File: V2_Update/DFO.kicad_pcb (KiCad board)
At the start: 2 copper layers, 19.8 x 19.6 mm, 18 parts, among them U1 Si5351A-B-GT, U2 ATmega328-A, X1 ASE-25MHz

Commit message: update
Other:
- board text added: "JP1"
- board text added: "JP2"
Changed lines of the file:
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@@
     (fp_line (start -0.261252 -0.735) (end 0.261252 -0.735) (layer "F.SilkS") (width 0.12))
     (fp_line (start -0.261252 0.735) (end 0.261252 0.735) (layer "F.SilkS") (width 0.12))
+    (fp_line (start -1.7 -0.98) (end 1.7 -0.98) (layer "F.CrtYd") (width 0.05))
+    (fp_line (start 1.7 0.98) (end -1.7 0.98) (layer "F.CrtYd") (width 0.05))
     (fp_line (start -1.7 0.98) (end -1.7 -0.98) (layer "F.CrtYd") (width 0.05))
     (fp_line (start 1.7 -0.98) (end 1.7 0.98) (layer "F.CrtYd") (width 0.05))
-    (fp_line (start 1.7 0.98) (end -1.7 0.98) (layer "F.CrtYd") (width 0.05))
-    (fp_line (start -1.7 -0.98) (end 1.7 -0.98) (layer "F.CrtYd") (width 0.05))
+    (fp_line (start 1 -0.625) (end 1 0.625) (layer "F.Fab") (width 0.1))
+    (fp_line (start -1 0.625) (end -1 -0.625) (layer "F.Fab") (width 0.1))
+    (fp_line (start 1 0.625) (end -1 0.625) (layer "F.Fab") (width 0.1))
     (fp_line (start -1 -0.625) (end 1 -0.625) (layer "F.Fab") (width 0.1))
-    (fp_line (start -1 0.625) (end -1 -0.625) (layer "F.Fab") (width 0.1))
-    (fp_line (start 1 -0.625) (end 1 0.625) (layer "F.Fab") (width 0.1))
-    (fp_line (start 1 0.625) (end -1 0.625) (layer "F.Fab") (width 0.1))
     (pad "1" smd roundrect (at -0.95 0 90) (size 1 1.45) (layers "F.Cu" "F.Paste" "F.Mask") (roundrect_rratio 0.25)
       (net 35 "CLK_OUT_SI5351"))
@@
     (fp_line (start -0.261252 -0.735) (end 0.261252 -0.735) (layer "F.SilkS") (width 0.12))
     (fp_line (start -0.261252 0.735) (end 0.261252 0.735) (layer "F.SilkS") (width 0.12))
+    (fp_line (start 1.7 -0.98) (end 1.7 0.98) (layer "F.CrtYd") (width 0.05))
+    (fp_line (start -1.7 -0.98) (end 1.7 -0.98) (layer "F.CrtYd") (width 0.05))
+    (fp_line (start 1.7 0.98) (end -1.7 0.98) (layer "F.CrtYd") (width 0.05))
     (fp_line (start -1.7 0.98) (end -1.7 -0.98) (layer "F.CrtYd") (width 0.05))
-    (fp_line (start 1.7 -0.98) (end 1.7 0.98) (layer "F.CrtYd") (width 0.05))
-    (fp_line (start 1.7 0.98) (end -1.7 0.98) (layer "F.CrtYd") (width 0.05))
-    (fp_line (start -1.7 -0.98) (end 1.7 -0.98) (layer "F.CrtYd") (width 0.05))
+    (fp_line (start -1 0.625) (end -1 -0.625) (layer "F.Fab") (width 0.1))
     (fp_line (start -1 -0.625) (end 1 -0.625) (layer "F.Fab") (width 0.1))
-    (fp_line (start -1 0.625) (end -1 -0.625) (layer "F.Fab") (width 0.1))
     (fp_line (start 1 -0.625) (end 1 0.625) (layer "F.Fab") (width 0.1))
     (fp_line (start 1 0.625) (end -1 0.625) (layer "F.Fab") (width 0.1))
@@
     (fp_line (start -0.261252 -0.735) (end 0.261252 -0.735) (layer "F.SilkS") (width 0.12))
     (fp_line (start -0.261252 0.735) (end 0.261252 0.735) (layer "F.SilkS") (width 0.12))
+    (fp_line (start -1.7 0.98) (end -1.7 -0.98) (layer "F.CrtYd") (width 0.05))
     (fp_line (start 1.7 -0.98) (end 1.7 0.98) (layer "F.CrtYd") (width 0.05))
-    (fp_line (start -1.7 0.98) (end -1.7 -0.98) (layer "F.CrtYd") (width 0.05))
     (fp_line (start 1.7 0.98) (end -1.7 0.98) (layer "F.CrtYd") (width 0.05))
     (fp_line (start -1.7 -0.98) (end 1.7 -0.98) (layer "F.CrtYd") (width 0.05))
+    (fp_line (start 1 -0.625) (end 1 0.625) (layer "F.Fab") (width 0.1))
+    (fp_line (start 1 0.625) (end -1 0.625) (layer "F.Fab") (width 0.1))
     (fp_line (start -1 0.625) (end -1 -0.625) (layer "F.Fab") (width 0.1))
     (fp_line (start -1 -0.625) (end 1 -0.625) (layer "F.Fab") (width 0.1))
-    (fp_line (start 1 0.625) (end -1 0.625) (layer "F.Fab") (width 0.1))
-    (fp_line (start 1 -0.625) (end 1 0.625) (layer "F.Fab") (width 0.1))
     (pad "1" smd roundrect (at -0.95 0) (size 1 1.45) (layers "F.Cu" "F.Paste" "F.Mask") (roundrect_rratio 0.25))
     (pad "2" smd roundrect (at 0.95 0) (size 1 1.45) (layers "F.Cu" "F.Paste" "F.Mask") (roundrect_rratio 0.25)
@@
       (effects (font (size 0.5 0.5) (thickness 0.08)))
     )
+    (fp_line (start -0.261252 0.735) (end 0.261252 0.735) (layer "F.SilkS") (width 0.12))
     (fp_line (start -0.261252 -0.735) (end 0.261252 -0.735) (layer "F.SilkS") (width 0.12))
-    (fp_line (start -0.261252 0.735) (end 0.261252 0.735) (layer "F.SilkS") (width 0.12))
-    (fp_line (start -1.7 0.98) (end -1.7 -0.98) (layer "F.CrtYd") (width 0.05))
+    (fp_line (start -1.7 -0.98) (end 1.7 -0.98) (layer "F.CrtYd") (width 0.05))
     (fp_line (start 1.7 0.98) (end -1.7 0.98) (layer "F.CrtYd") (width 0.05))
     (fp_line (start 1.7 -0.98) (end 1.7 0.98) (layer "F.CrtYd") (width 0.05))
-    (fp_line (start -1.7 -0.98) (end 1.7 -0.98) (layer "F.CrtYd") (width 0.05))
+    (fp_line (start -1.7 0.98) (end -1.7 -0.98) (layer "F.CrtYd") (width 0.05))
+    (fp_line (start -1 -0.625) (end 1 -0.625) (layer "F.Fab") (width 0.1))
+    (fp_line (start 1 -0.625) (end 1 0.625) (layer "F.Fab") (width 0.1))
+    (fp_line (start 1 0.625) (end -1 0.625) (layer "F.Fab") (width 0.1))
     (fp_line (start -1 0.625) (end -1 -0.625) (layer "F.Fab") (width 0.1))
-    (fp_line (start 1 -0.625) (end 1 0.625) (layer "F.Fab") (width 0.1))
-    (fp_line (start -1 -0.625) (end 1 -0.625) (layer "F.Fab") (width 0.1))
-    (fp_line (start 1 0.625) (end -1 0.625) (layer "F.Fab") (width 0.1))
     (pad "1" smd roundrect (at -0.95 0) (size 1 1.45) (layers "F.Cu" "F.Paste" "F.Mask") (roundrect_rratio 0.25)
       (net 30 "i2c-SCL"))
@@
       (effects (font (size 1 1) (thickness 0.15)) (justify mirror))
     )
+    (fp_line (start 1.4 1) (end 1.4 -1) (layer "B.SilkS") (width 0.12))
+    (fp_line (start -1.4 1) (end 1.4 1) (layer "B.SilkS") (width 0.12))
+    (fp_line (start -1.4 -1) (end -1.4 1) (layer "B.SilkS") (width 0.12))
     (fp_line (start 1.4 -1) (end -1.4 -1) (layer "B.SilkS") (width 0.12))
-    (fp_line (start -1.4 -1) (end -1.4 1) (layer "B.SilkS") (width 0.12))
-    (fp_line (start -1.4 1) (end 1.4 1) (layer "B.SilkS") (width 0.12))
-    (fp_line (start 1.4 1) (end 1.4 -1) (layer "B.SilkS") (width 0.12))
+    (fp_line (start -1.65 1.25) (end 1.65 1.25) (layer "B.CrtYd") (width 0.05))
+    (fp_line (start 1.65 -1.25) (end -1.65 -1.25) (layer "B.CrtYd") (width 0.05))
+    (fp_line (start 1.65 -1.25) (end 1.65 1.25) (layer "B.CrtYd") (width 0.05))
     (fp_line (start -1.65 1.25) (end -1.65 -1.25) (layer "B.CrtYd") (width 0.05))
-    (fp_line (start 1.65 -1.25) (end -1.65 -1.25) (layer "B.CrtYd") (width 0.05))
-    (fp_line (start -1.65 1.25) (end 1.65 1.25) (layer "B.CrtYd") (width 0.05))
-    (fp_line (start 1.65 -1.25) (end 1.65 1.25) (layer "B.CrtYd") (width 0.05))
     (pad "1" smd rect (at -0.65 0 270) (size 1 1.5) (layers "B.Cu" "B.Mask")
       (net 32 "CLKOUT"))
@@
       (effects (font (size 1 1) (thickness 0.15)) (justify mirror))
     )
+    (fp_line (start -1.4 -1) (end -1.4 1) (layer "B.SilkS") (width 0.12))
     (fp_line (start 1.4 -1) (end -1.4 -1) (layer "B.SilkS") (width 0.12))
-    (fp_line (start -1.4 -1) (end -1.4 1) (layer "B.SilkS") (width 0.12))
+    (fp_line (start 1.4 1) (end 1.4 -1) (layer "B.SilkS") (width 0.12))
     (fp_line (start -1.4 1) (end 1.4 1) (layer "B.SilkS") (width 0.12))
-    (fp_line (start 1.4 1) (end 1.4 -1) (layer "B.SilkS") (width 0.12))
+    (fp_line (start -1.65 1.25) (end 1.65 1.25) (layer "B.CrtYd") (width 0.05))
     (fp_line (start -1.65 1.25) (end -1.65 -1.25) (layer "B.CrtYd") (width 0.05))
     (fp_line (start 1.65 -1.25) (end -1.65 -1.25) (layer "B.CrtYd") (width 0.05))
-    (fp_line (start -1.65 1.25) (end 1.65 1.25) (layer "B.CrtYd") (width 0.05))
     (fp_line (start 1.65 -1.25) (end 1.65 1.25) (layer "B.CrtYd") (width 0.05))
     (pad "1" smd rect (at -0.65 0 180) (size 1 1.5) (layers "B.Cu" "B.Mask")
@@
   (gr_line (start 92.12 79) (end 92.200583 59.42) (layer "Edge.Cuts") (width 0.1))
   (gr_line (start 92.200583 59.42) (end 111.9 59.35) (layer "Edge.Cuts") (width 0.1))
+  (gr_text "JP2\n" (at 104.648 76.708) (layer "B.SilkS")
+    (effects (font (size 1.5 1) (thickness 0.25)) (justify mirror))
+  )
   (gr_text "JP1: REF CLK PIN 1 GND" (at 97.028 61.976) (layer "B.SilkS")
     (effects (font (size 1.5 0.5) (thickness 0.125)) (justify mirror))
@@
     (effects (font (size 1.5 0.5) (thickness 0.125)) (justify mirror))
   )
+  (gr_text "JP1\n" (at 104.394 74.422) (layer "B.SilkS")
+    (effects (font (size 1.5 1) (thickness 0.25)) (justify mirror))
+  )
   (gr_text "JP3: DIRECT CLOCK OUT" (at 97.028 66.04) (layer "B.SilkS")

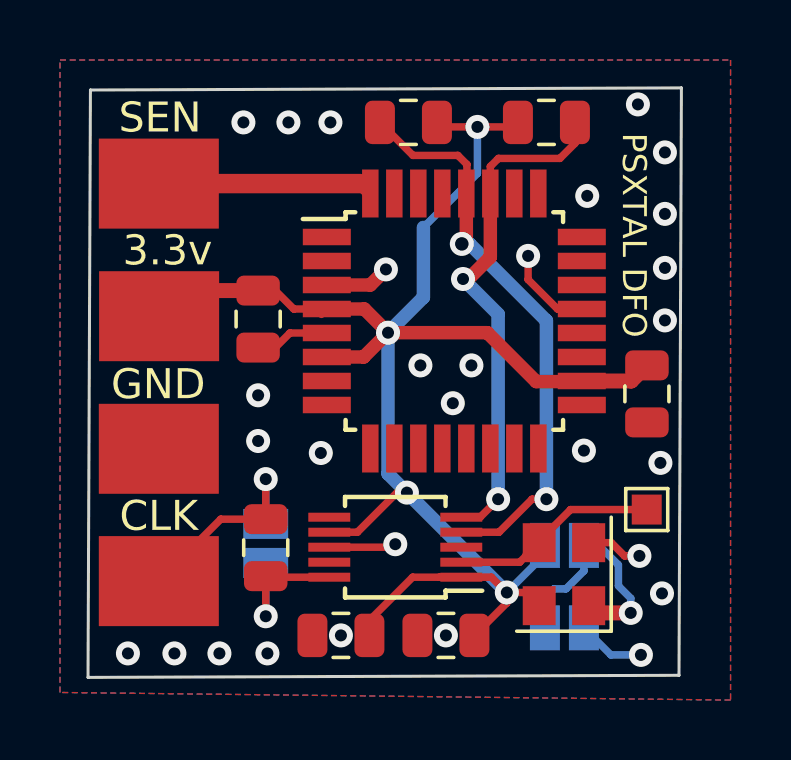
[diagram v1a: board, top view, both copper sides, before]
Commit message: fixed 2 GND points PCB
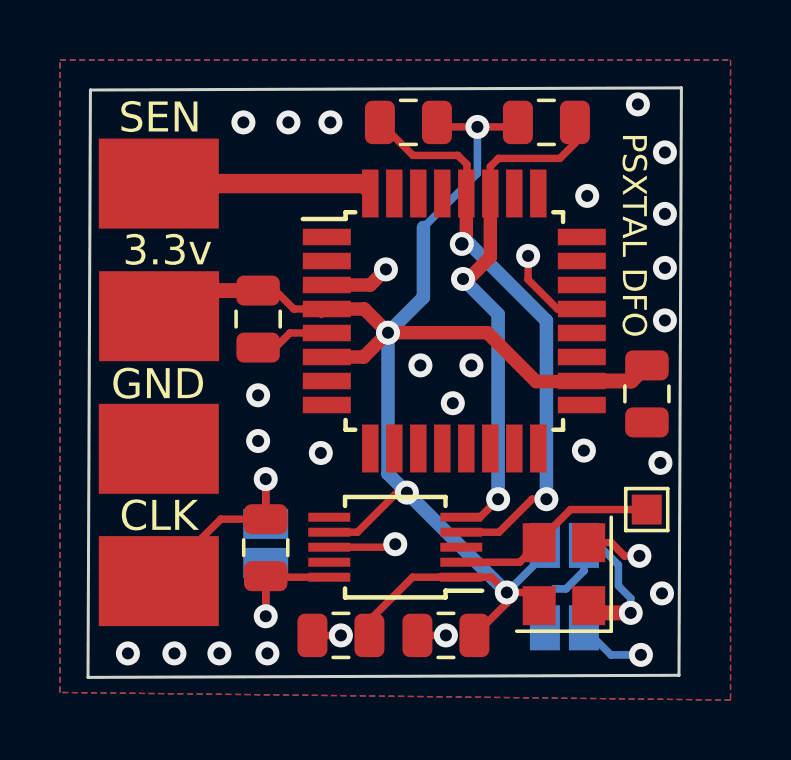
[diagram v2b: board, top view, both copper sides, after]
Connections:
- REF** pad 1: (no net) -> GND
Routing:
- net GND: track 14.3 -> 16.2 mm
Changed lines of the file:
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@@
     (fp_line (start -1 0.625) (end -1 -0.625) (layer "F.Fab") (width 0.1))
     (fp_line (start -1 -0.625) (end 1 -0.625) (layer "F.Fab") (width 0.1))
-    (pad "1" smd roundrect (at -0.95 0) (size 1 1.45) (layers "F.Cu" "F.Paste" "F.Mask") (roundrect_rratio 0.25))
+    (pad "1" smd roundrect (at -0.95 0) (size 1 1.45) (layers "F.Cu" "F.Paste" "F.Mask") (roundrect_rratio 0.25)
+      (net 4 "GND"))
     (pad "2" smd roundrect (at 0.95 0) (size 1 1.45) (layers "F.Cu" "F.Paste" "F.Mask") (roundrect_rratio 0.25)
       (net 1 "+3.3V"))
@@
   (segment (start 97.79 68.006) (end 98.364 68.006) (width 0.25) (layer "F.Cu") (net 4))
   (segment (start 109.562 74.51) (end 110.002 74.95) (width 0.25) (layer "F.Cu") (net 4))
+  (segment (start 99.6 77.6) (end 100.55 77.6) (width 0.25) (layer "F.Cu") (net 4))
+  (segment (start 103.1 77.6) (end 104.05 77.6) (width 0.25) (layer "F.Cu") (net 4))
   (segment (start 108.809998 74.51) (end 109.562 74.51) (width 0.25) (layer "F.Cu") (net 4))
   (segment (start 98.364 68.006) (end 98.85 67.52) (width 0.25) (layer "F.Cu") (net 4))
